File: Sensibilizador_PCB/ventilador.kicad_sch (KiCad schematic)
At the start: 2 parts, among them M1 Fan, Q5 SI2302

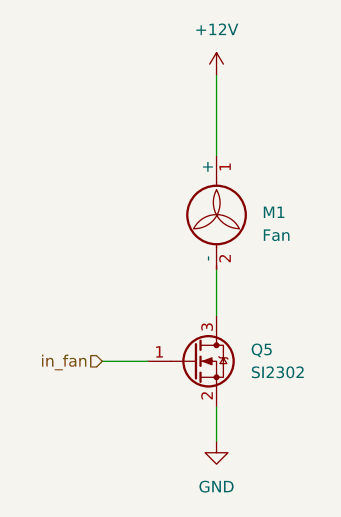
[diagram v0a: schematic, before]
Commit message: ValoresCorregidos
Algunos valores de resistencias fueron corregidos y coinciden con la placa.
Valores de resistencias en los leds.
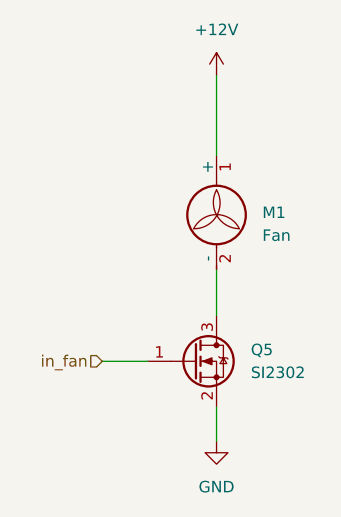
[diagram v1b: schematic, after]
